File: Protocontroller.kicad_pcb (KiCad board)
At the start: 4 copper layers, 51 x 26.4 mm, 39 parts, among them U1 AP2112K-3.3TRG1, U2 PM254-1-14-Z-8.5, U3 PM254-1-14-Z-8.5, U4 74245PW, U5 74245PW, U6 74374PW, U8 HC-JN254-2-08-W

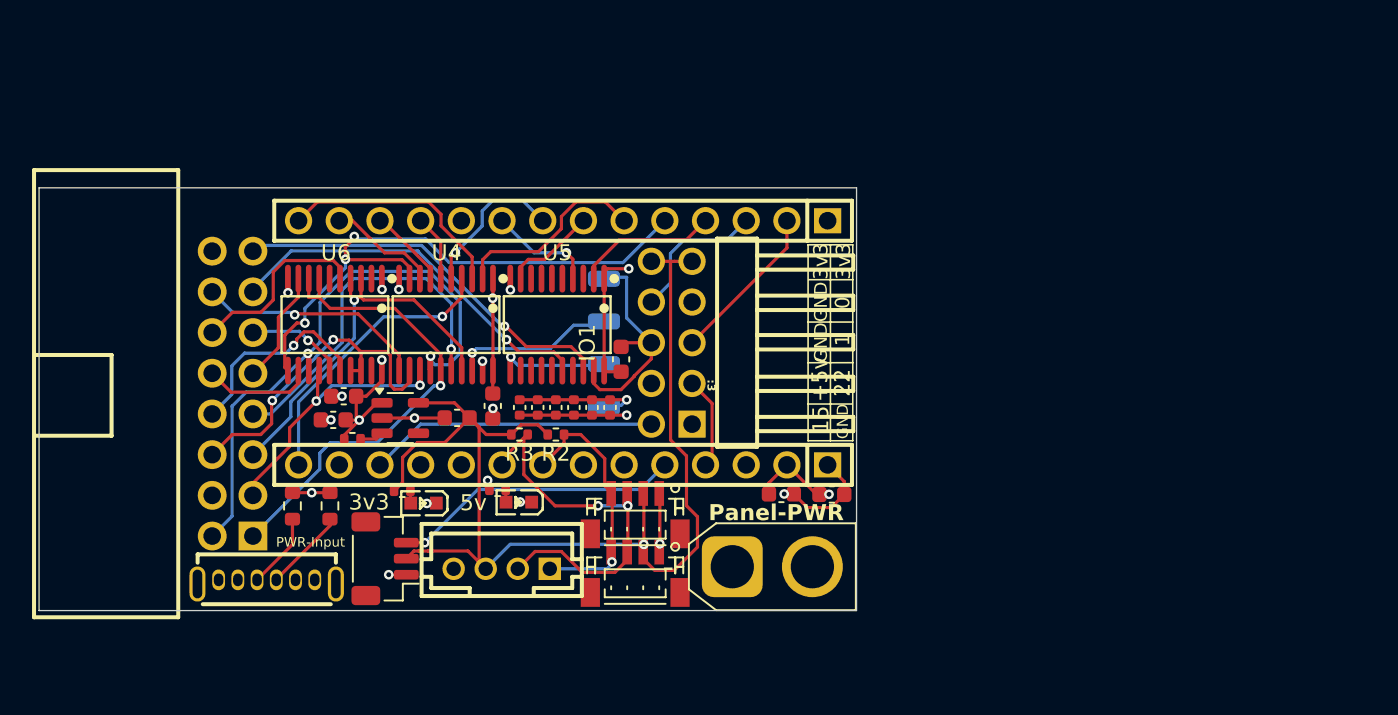
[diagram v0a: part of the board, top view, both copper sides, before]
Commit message: V2 of the neo released, switched stemma to stemma qt, adjusted io pinout, replaced secondary 74245 with the 7408, swapped apaclk and apadat, switched to 2 layer for cheaper costs, esp32 schematic in, in unused, dedicated fan header,
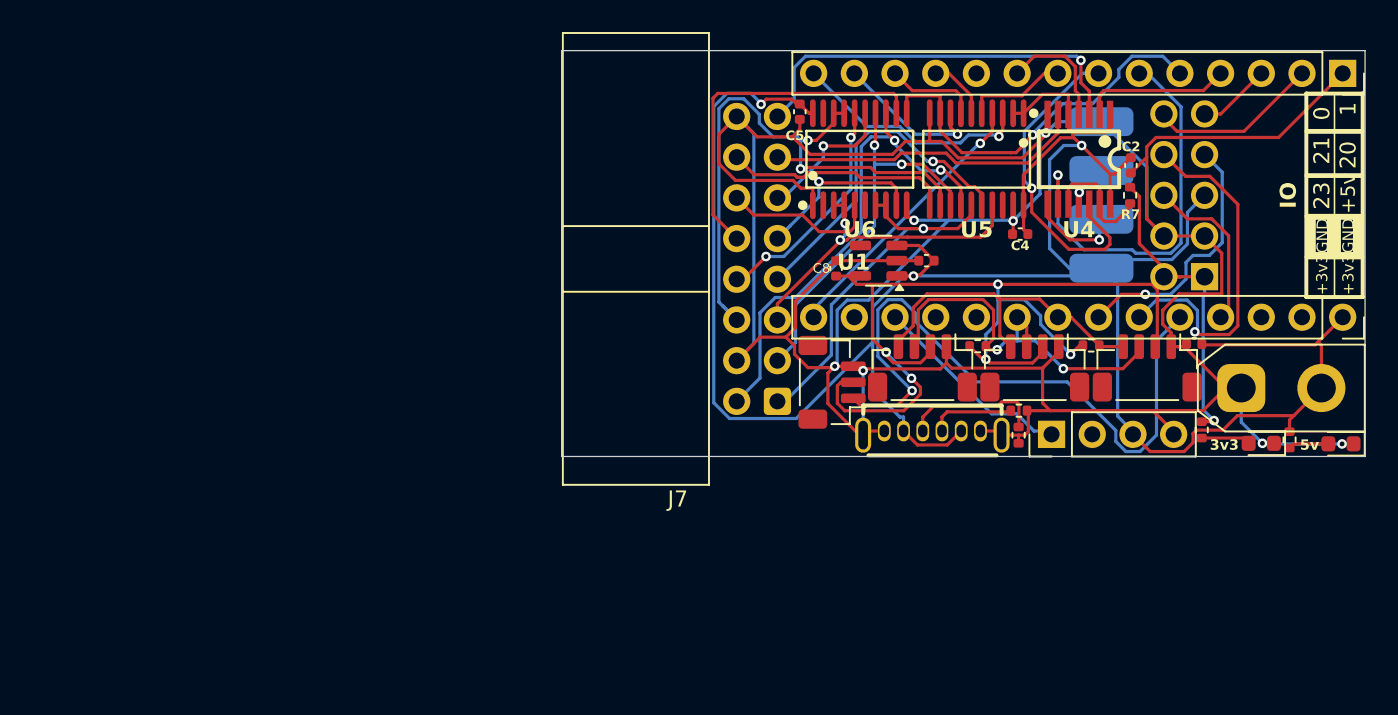
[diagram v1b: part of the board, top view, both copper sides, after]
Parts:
- removed 3v3, 5v: XL-1608UVC-04, Protocontroller:LED0603-RD_PINK
- removed APA102-Pad1: ~, Connector_Wire:JST-SM 4P PAD
- removed C1, C6, C7: 10uF, Capacitor_SMD:C_0603_1608Metric
- removed C10, C11, C12, C13, C9: 22uF, Capacitor_SMD:C_0402_1005Metric
- removed LOGO, QR: LOGO, LOGO
- removed Mic: BM03B-SRSS-TB(LF)(SN), Connector_JST:JST_SH_BM03B-SRSS-TB_1x03-1MP_P1.00mm_Vertical
- removed PWR-Input: TYPE-C 16PFS LCH7.45 IPX8, Protocontroller:USB-C-TH_TYPE-C-6PLCH10.0-073
- removed Panel-PWR: XT30U-M, Connector_AMASS:AMASS_XT30U-M_1x02_P5.0mm_Vertical
- removed R5: 10K_0201, Resistor_SMD:R_0402_1005Metric
- removed R6: 5.1K_0603, Resistor_SMD:R_0603_1608Metric
- removed U2, U3: PM254-1-14-Z-8.5, Protocontroller:HDR-TH_14P-P2.54-V-F-1
- removed U8: HC-JN254-2-08-W, Protocontroller:HDR-TH_16P-P2.54-H-F-R2-C8-W9.0
- added AxionLogo: LOGO, LOGO, B.Cu at (113.8, 30.0)
- added C14: 1uF_0402, Capacitor_SMD:C_0402_1005Metric, F.Cu at (132.7, 35.0)
- added D1: LED, LED_SMD:LED_0603_1608Metric, F.Cu at (153.6, 46.4)
- added D2: LED, LED_SMD:LED_0603_1608Metric, F.Cu at (158.6, 46.5)
- added FanHeader1: Conn_01x04, Connector_PinHeader_2.54mm:PinHeader_1x04_P2.54mm_Vertical, F.Cu at (140.5, 45.9)
- added G***: LOGO, LOGO, B.Cu at (155.6, 30.8)
- added J2: Conn_01x14_Socket, Connector_PinSocket_2.54mm:PinSocket_1x14_P2.54mm_Vertical, F.Cu at (158.7, 23.3)
- added J3: Conn_01x14_Socket, Connector_PinSocket_2.54mm:PinSocket_1x14_P2.54mm_Vertical, F.Cu at (158.7, 38.6)
- added J4: Conn_01x04, Connector_Wire:JST_SM 1x04 Pad, F.Cu at (143.6, 30.9)
- added J7: Conn_02x08_Odd_Even, Connector_IDC:IDC-Header_2x08_P2.54mm_Horizontal, F.Cu at (123.4, 43.8)
- added Mic1: BM03B-SRSS-TB(LF)(SN), Connector_JST:JST_SH_BM03B-SRSS-TB_1x03-1MP_P1.00mm_Vertical, F.Cu at (126.8, 42.6)
- added PWRINPUT1: USB-C-TH_TYPE-C-6PLCH10.0-073, Protocontroller:USB-C-TH_TYPE-C-6PLCH10.0-073, F.Cu at (133.1, 45.8)
- added PanelPWR1: XT30UPB-M, Connector_AMASS:AMASS_XT30UPB-M_1x02_P5.0mm_Vertical, F.Cu at (152.4, 43.0)
- added Qr: LOGO, LOGO, B.Cu at (113.6, 43.5)
- added R11: 10K_0402, Resistor_SMD:R_0402_1005Metric, F.Cu at (155.4, 46.2)
- added R8: 5.1K_0402, Resistor_SMD:R_0402_1005Metric, F.Cu at (149.9, 45.6)
- C2, C5: value 10uF -> 0.1uF_0402; footprint Capacitor_SMD:C_0603_1608Metric -> Capacitor_SMD:C_0402_1005Metric
- C3: value 22uF -> 10uF_0402; footprint Capacitor_SMD:C_0603_1608Metric -> Capacitor_SMD:C_0402_1005Metric
- C4: value 0.1uF -> 0.1uF_0402; footprint Capacitor_SMD:C_0603_1608Metric -> Capacitor_SMD:C_0402_1005Metric
- C8: value 22uF -> 10uF_0402
- I2C-1, I2C-2: footprint Protocontroller:CONN-SMD_BM04B-SRSS-TB -> Connector_JST:JST_SH_BM04B-SRSS-TB_1x04-1MP_P1.00mm_Vertical
- I2C-3: value B4B-PH-K-K(LF)(SN) -> BM04B-SRSS-TB(LF)(SN); footprint Protocontroller:CONN-TH_B4B-PH-K-S-LF-SN -> Connector_JST:JST_SH_BM04B-SRSS-TB_1x04-1MP_P1.00mm_Vertical
- IO1: value 2541WR-2X05P -> PINHD_2x5_Male
- R1, R4: value 10K_0201 -> 5.1K_0402
- R2: value 4.7K_402 -> 4.7K_0402
- R7: value 5.1K_0603 -> 47K_0402; footprint Resistor_SMD:R_0603_1608Metric -> Resistor_SMD:R_0402_1005Metric
- U4: value 74245PW -> SN74AHCT08PWR; footprint Protocontroller:SN74AHCT245PWR -> Protocontroller:TSSOP-14_L5.0-W4.4-P0.65-LS6.4-BL
- U5: value 74245PW -> SN74AHCT245PWR; footprint Protocontroller:SN74AHCT245PWR -> Protocontroller:TSSOP-20_L6.5-W4.4-P0.65-LS6.4-BL
- U6: value 74374PW -> 74AHCT374
- moved R7 53.6 mm to (145.4, 31.0), turned to 90 degrees
- moved C2 44.9 mm to (145.5, 29.1), turned to 90 degrees
- moved R1 41.6 mm to (138.5, 45.9), turned to 90 degrees
- moved U4 40.8 mm to (142.2, 28.7)
- moved R4 38.8 mm to (138.5, 44.4)
- moved U6 34.3 mm to (128.6, 28.7), turned to 0 degrees
- moved R2 33.9 mm to (143.0, 40.3)
- moved IO1 33.3 mm to (148.8, 30.9)
- moved I2C-1 33.2 mm to (146.5, 41.7)
- moved U1 31.4 mm to (129.7, 35.0), turned to 180 degrees
- moved R3 29.1 mm to (135.9, 40.4)
- moved I2C-3 29.1 mm to (132.5, 41.7), turned to 180 degrees
- moved U5 28.1 mm to (135.9, 28.7)
- moved I2C-2 28.0 mm to (139.5, 41.7)
- moved C3 27.4 mm to (149.4, 40.2), turned to 0 degrees
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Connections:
- C2 pad 1: +3.3V -> GND
- C2 pad 2: GND -> +5V
- C3 pad 1: +5V -> GND
- C3 pad 2: GND -> +5V
- C4 pad 1: +5V -> GND
- C4 pad 2: GND -> +5V
- C8 pad 1: +5V -> +3.3V
- I2C-1 pad 3: /TSDA0 -> /SDA
- I2C-1 pad 4: /TSCL0 -> /SCL
- I2C-2 pad 3: /TSDA0 -> /SDA
- I2C-2 pad 4: /TSCL0 -> /SCL
- I2C-3 pad 1: /TSCL0 -> GND
- I2C-3 pad 2: /TSDA0 -> +3.3V
- I2C-3 pad 3: +3.3V -> /SDA
- I2C-3 pad 4: GND -> /SCL
- IO1 pad 1: GND -> +3.3V
- IO1 pad 10: +3.3V -> /RX
- IO1 pad 2: /TPWM1 -> +3.3V
- IO1 pad 3: /ANALOG2 -> GND
- IO1 pad 4: +5V -> GND
- IO1 pad 5: /DIGITAL1 -> +5V
- IO1 pad 6: GND -> /Analog1
- IO1 pad 7: GND -> /Digital2
- IO1 pad 8: /DIGITAL2 -> /Digital1
- IO1 pad 9: +3.3V -> /TX
- R1 pad 1: +5V -> GND
- R1 pad 2: Net-(U1-EN) -> Net-(PWRINPUT1-CC2)
- R2 pad 1: /TSCL0 -> /SCL
- R3 pad 1: /TSDA0 -> /SDA
- R4 pad 1: +3.3V -> Net-(PWRINPUT1-CC1)
- R4 pad 2: Net-(3v1-A) -> GND
- R7 pad 1: GND -> Net-(U4-3B)
- R7 pad 2: Net-(PWR-Input1-CC1) -> +3.3V
- U1 pad 3: Net-(U1-EN) -> +5V
- U4 pad 10: GND -> Net-(U4-3B)
- U4 pad 11: /PANEL_LATCH -> /APA_DAT
- U4 pad 12: /PANEL_G2 -> /FLEXIO_MOSI
- U4 pad 13: /PANEL_B1 -> Net-(U4-3B)
- U4 pad 14: /PANEL_G1 -> +5V
- U4 pad 2: /FLEXIO_SCK -> /BUFFER_OE
- U4 pad 3: /BUFFER_R2 -> /PANEL_OE
- U4 pad 4: /BUFFER_B2/SCK -> /BUFFER_CLK
- U4 pad 5: /BUFFER_R1 -> +5V
- U4 pad 6: /BUFFER_G1 -> /PANEL_CLK
- U4 pad 7: /BUFFER_B1 -> GND
- U4 pad 8: /BUFFER_G2/MOSI -> /APA_CLK
- U4 pad 9: /BUFFER_LATCH -> /FLEXIO_SCK
- U5 pad 11: /APA_DAT -> /PANEL_LATCH
- U5 pad 12: unconnected-(U5-B7-Pad12) -> /PANEL_G2
- U5 pad 13: unconnected-(U5-B6-Pad13) -> /PANEL_B1
- U5 pad 14: unconnected-(U5-B5-Pad14) -> /PANEL_G1
- U5 pad 15: unconnected-(U5-B4-Pad15) -> /PANEL_R1
- U5 pad 16: /PANEL_CLK -> /PANEL_B2
- U5 pad 17: unconnected-(U5-B2-Pad17) -> /PANEL_R2
- U5 pad 18: /PANEL_OE -> unconnected-(U5-B1-Pad18)
- U5 pad 2: /BUFFER_OE -> +5V
- U5 pad 3: unconnected-(U5-A2-Pad3) -> /BUFFER_R2
- U5 pad 4: /BUFFER_CLK -> /BUFFER_B2
- U5 pad 5: unconnected-(U5-A4-Pad5) -> /BUFFER_R1
- U5 pad 6: unconnected-(U5-A5-Pad6) -> /BUFFER_G1
- U5 pad 7: unconnected-(U5-A6-Pad7) -> /BUFFER_B1
- U5 pad 8: unconnected-(U5-A7-Pad8) -> /BUFFER_G2
- U5 pad 9: /FLEXIO_MOSI -> /BUFFER_LATCH
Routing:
- net GND: track 46.9 -> 214.7 mm, vias 16 -> 7
- net +5V: track 58.0 -> 156.5 mm, vias 7 -> 3
- net /Mic1: track 0.00 -> 40.9 mm, vias 0 -> 1
- net /SDA: track 0.00 -> 25.0 mm, vias 0 -> 2
- net /TSDA0: track 24.8 -> 0.00 mm, vias 2 -> 0
- net /Digital1: track 0.00 -> 22.2 mm, vias 0 -> 1
- net /SCL: track 0.00 -> 20.9 mm
- net /ANALOG1: track 18.1 -> 0.00 mm, vias 1 -> 0
- net /TPWM1: track 18.0 -> 0.00 mm
- net /BUFFER_B2/SCK: track 18.0 -> 0.00 mm, vias 1 -> 0
- net /BUFFER_B2: track 0.00 -> 17.4 mm, vias 0 -> 1
- net /PANEL_G2: track 21.3 -> 38.3 mm
- net /TSCL0: track 16.4 -> 0.00 mm, vias 1 -> 0
- net /Digital2: track 0.00 -> 16.2 mm, vias 0 -> 1
- net /PANEL_ADX1: track 6.89 -> 23.0 mm
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- removed copper zone on In2.Cu, net +5V
- removed copper zone on In1.Cu, net GND
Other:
- board size 51 x 26.4 mm -> 50.1 x 25.3 mm
- copper layers 4 -> 2
- board text added: "+3v3"
- board text added: "20"
- board text added: "21"
- board text added: "23"
- board text added: "5v"
- board text added: "Fan"
- board text added: "IO"
- board text added: "Mic"
- board text added: "PWR Input"
- board text added: "Panel PWR"
- board text removed: "+5V"
- board text removed: "15"
- board text removed: "22"
- board text removed: "AxionQc"
- board text removed: "AxionQc.dev"

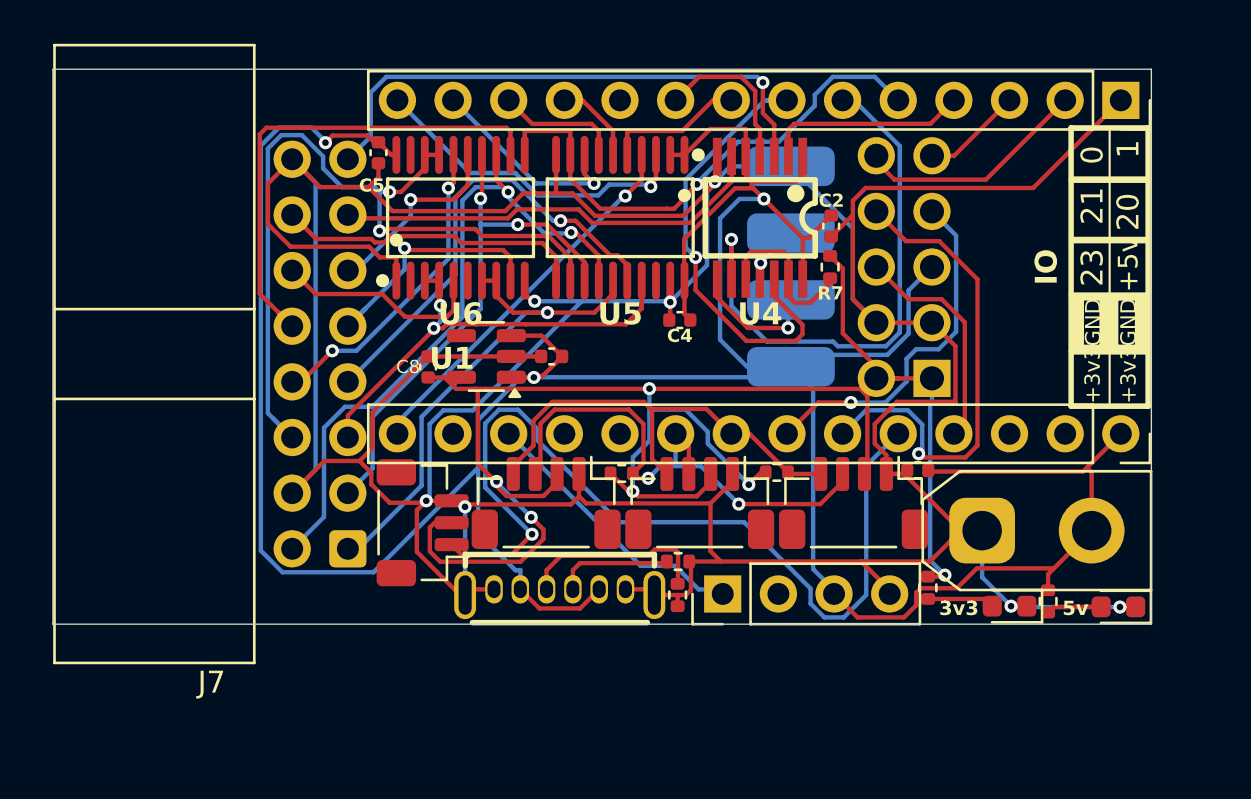
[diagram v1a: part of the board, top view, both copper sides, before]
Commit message: new layout, bunch of empty space
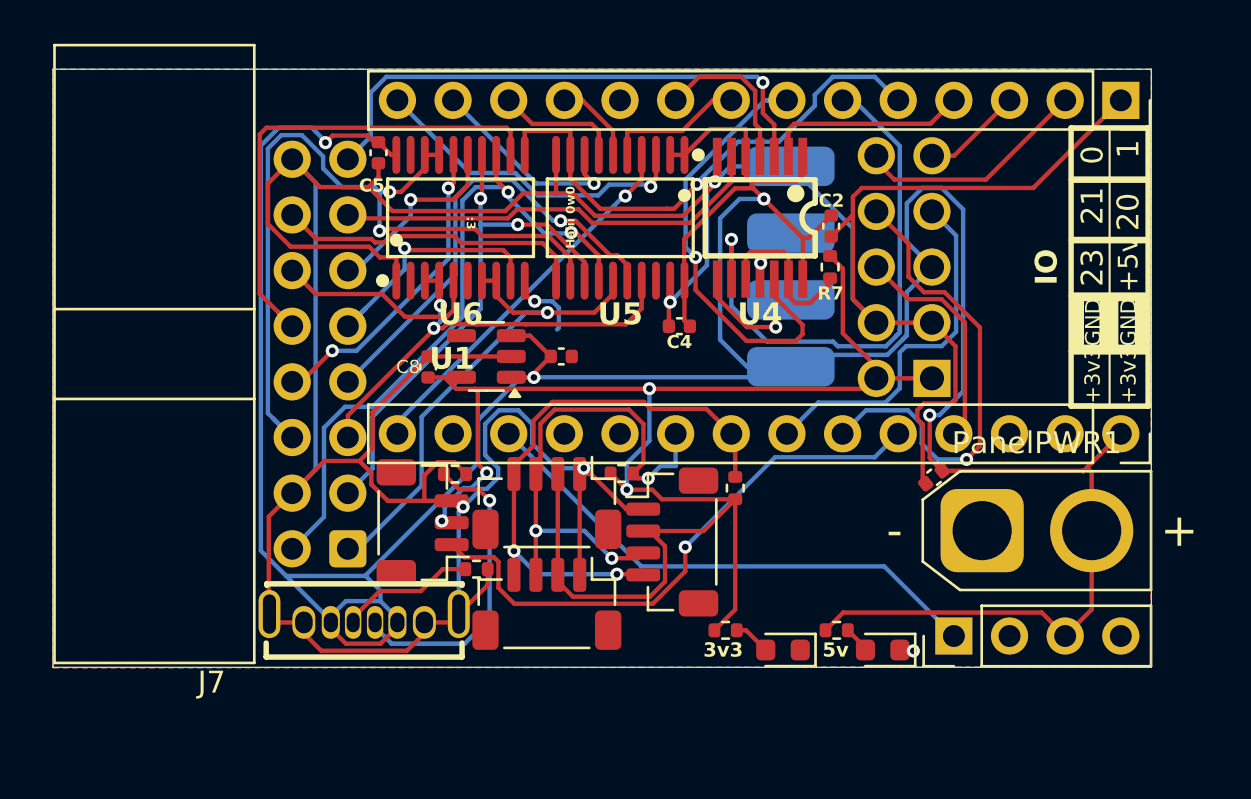
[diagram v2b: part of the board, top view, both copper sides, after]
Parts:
- PWRINPUT1: footprint Protocontroller:USB-C-TH_TYPE-C-6PLCH10.0-073 -> Protocontroller:USB-C-TH_TYPE-C-6P-LC6.8-073
- PanelPWR1: value XT30UPB-M -> XT30U-M; footprint Connector_AMASS:AMASS_XT30UPB-M_1x02_P5.0mm_Vertical -> Connector_AMASS:AMASS_XT30U-M_1x02_P5.0mm_Vertical
- R8: value 5.1K_0402 -> 10K_0402
- moved D2 10.9 mm to (147.8, 48.4)
- moved R4 10.9 mm to (128.3, 40.4)
- moved FanHeader1 10.7 mm to (151.1, 47.8)
- moved D1 10.5 mm to (143.3, 48.4)
- moved R11 9.74 mm to (145.7, 47.5), turned to 0 degrees
- moved R8 9.44 mm to (140.7, 47.5), turned to 0 degrees
- moved R1 9.26 mm to (129.3, 44.7), turned to 180 degrees
- moved PWRINPUT1 9.01 mm to (124.2, 47.0)
- moved I2C-1 8.46 mm to (138.2, 43.5), turned to -90 degrees
- moved I2C-2 8.36 mm to (132.5, 46.3)
- moved R2 2.03 mm to (141.1, 41.0), turned to -90 degrees
- moved C3 0.80 mm to (150.2, 40.5), turned to 38 degrees
- moved C14 0.44 mm to (133.2, 35.0), turned to 0 degrees
- moved C4 0.28 mm to (138.6, 33.6)
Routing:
- net GND: track 214.7 -> 179.4 mm, vias 7 -> 6
- net /Mic1: track 40.9 -> 26.1 mm
- net +5V: track 156.5 -> 168.0 mm, vias 3 -> 4
- net /PWM: track 12.7 -> 24.1 mm
- net +3.3V: track 83.7 -> 73.9 mm, vias 6 -> 4
- net Net-(PWRINPUT1-CC1): track 5.33 -> 14.2 mm, vias 0 -> 1
- net /SCL: track 20.9 -> 25.8 mm, vias 0 -> 2
- net Net-(PWRINPUT1-CC2): track 8.75 -> 6.25 mm
- net Net-(D1-A): track 3.30 -> 1.70 mm
- net Net-(D2-A): track 2.53 -> 1.23 mm
- net /SDA: track 25.0 -> 24.0 mm, vias 2 -> 3
- net /APA_CLK: track 6.28 -> 5.60 mm
- net /Digital1: track 22.2 -> 21.6 mm
- net /Digital2: track 16.2 -> 16.6 mm, vias 1 -> 0
- added copper zone on B.Cu, net GND
- added copper zone on F.Cu, net GND
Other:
- board size 50.1 x 25.3 mm -> 50.1 x 27.3 mm
- board text added: "Haiii 0w0"

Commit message: fix files
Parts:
- removed PWRINPUT1: USB-C-TH_TYPE-C-6PLCH10.0-073, Protocontroller:USB-C-TH_TYPE-C-6P-LC6.8-073
- added J1: USB_C_Receptacle_USB2.0_16P, Protocontroller:USB-TH_TYPE-C-16PFS-LCH7.45-IPX8, F.Cu at (124.5, 47.5)
- C2, C4, C5: value 0.1uF_0402 -> 100nF_0402
- PanelPWR1: value XT30U-M -> XT30U-M.G.B
- moved D2 7.09 mm to (140.7, 48.5)
- moved D1 5.62 mm to (137.7, 48.5)
- moved R11 4.87 mm to (141.1, 46.0), turned to -90 degrees
- moved R8 4.38 mm to (136.4, 46.3), turned to -90 degrees
- moved Qr 2.54 mm to (113.6, 46.1)
- moved C2 1.50 mm to (145.4, 27.6)
- moved R1 1.42 mm to (130.3, 45.8), turned to -90 degrees
- moved I2C-2 1.00 mm to (132.6, 47.3)
- moved I2C-3 1.00 mm to (132.6, 42.7)
- moved J7 0.90 mm to (123.2, 44.7)
- moved C4 0.68 mm to (138.4, 33.0)
- moved R7 0.66 mm to (145.0, 31.4)
- moved R4 0.55 mm to (128.9, 40.4)
- moved FanHeader1 0.51 mm to (151.1, 48.3)
- moved C3 0.37 mm to (150.5, 40.4)
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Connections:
- I2C-1 pad MP: (no net) -> unconnected-(I2C-1-PadMP)_1
- I2C-2 pad MP: (no net) -> GND
- I2C-3 pad MP: (no net) -> unconnected-(I2C-3-PadMP)
- R7 pad 1: Net-(U4-3B) -> +3.3V
- R7 pad 2: +3.3V -> Net-(U4-3B)
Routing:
- net GND: track 179.4 -> 154.6 mm, vias 6 -> 14
- net +5V: track 168.0 -> 180.8 mm, vias 4 -> 6
- net /FLEXIO_SCK: track 25.5 -> 13.6 mm
- net /Digital1: track 21.6 -> 10.8 mm, vias 1 -> 0
- net /RX: track 11.5 -> 20.7 mm
- net /PANEL_G2: track 38.3 -> 30.2 mm, vias 2 -> 3
- net /PANEL_ADX0: track 11.9 -> 18.4 mm, vias 1 -> 0
- net Net-(J1-CC1): track 14.2 -> 8.94 mm
- net /FLEXIO_MOSI: track 21.4 -> 26.5 mm, vias 1 -> 3
- net /SDA: track 24.0 -> 19.0 mm, vias 3 -> 2
- net /PANEL_B2: track 21.7 -> 16.8 mm, vias 1 -> 3
- net +3.3V: track 73.9 -> 70.4 mm
- net /Mic1: track 26.1 -> 23.0 mm, vias 1 -> 2
- net Net-(U4-3B): track 7.59 -> 10.5 mm, vias 0 -> 2
- net /PANEL_ADX1: track 23.0 -> 20.4 mm, vias 0 -> 1
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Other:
- board size 50.1 x 27.3 mm -> 50.1 x 27.8 mm

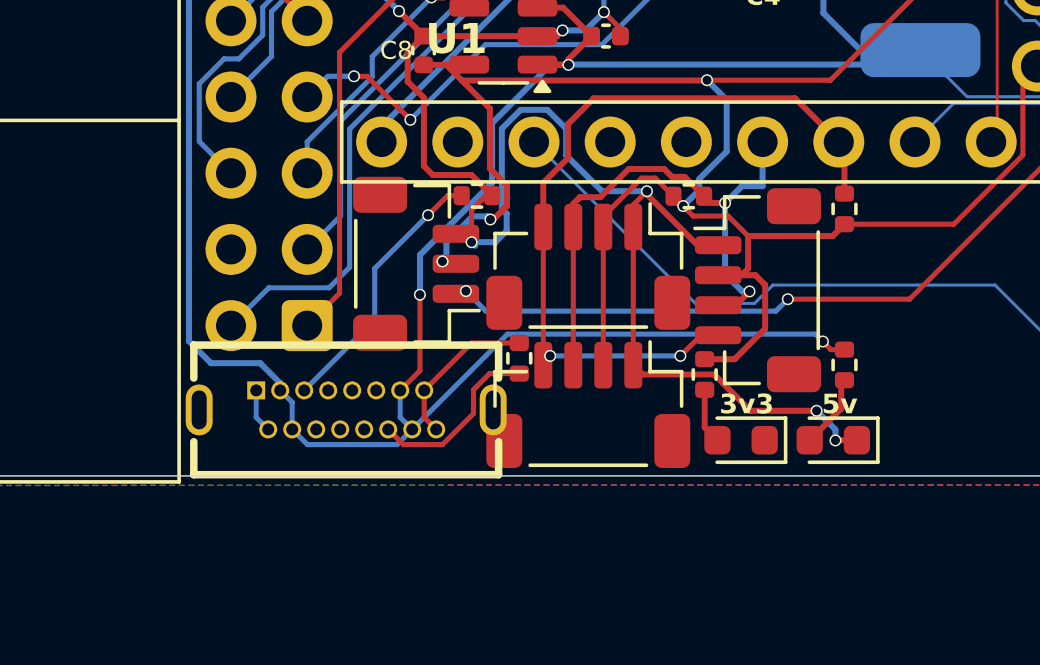
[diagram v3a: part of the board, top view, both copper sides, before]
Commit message: adjusted i2c position and ubc position
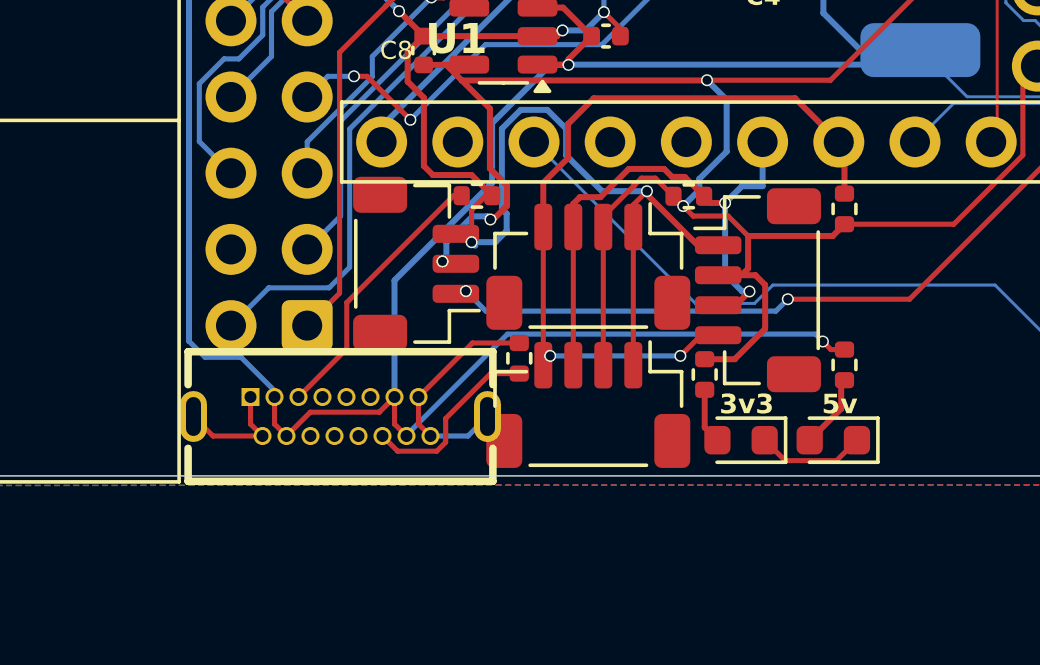
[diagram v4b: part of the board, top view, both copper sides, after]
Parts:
- moved I2C-2 4.61 mm to (132.6, 42.7)
- moved I2C-3 4.61 mm to (132.6, 47.3)
- moved J1 0.29 mm to (124.3, 47.7)
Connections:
- I2C-2 pad MP: GND -> unconnected-(I2C-2-PadMP)
- I2C-3 pad MP: unconnected-(I2C-3-PadMP) -> GND
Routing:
- net Net-(J1-CC1): track 8.94 -> 9.12 mm, vias 1 -> 0
- net +5V: track 180.8 -> 180.7 mm, vias 6 -> 5
- net GND: vias 14 -> 12
